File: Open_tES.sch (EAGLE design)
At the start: 60 parts, among them IC2 MAX232ECWES, IC4 LP2950CZ-5.0, IC5 OPA277U, IC6 LF444CM, IC7 PIC16F1937P, J1 RJ11-2X, U1 MIC2288YD5-TR, U2 74LVC1G10W6-7, X1 22-23-2041, X2 057-016-1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

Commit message: Removing input capacitor for LPO: C1_MIC already present.
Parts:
- removed C_LPO1: 1µF, rcl:C-EUC0805
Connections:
- net +9V: no longer C_LPO1.1
- net GND: no longer C_LPO1.2
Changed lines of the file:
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@@
 </part>
 <part name="SUPPLY8" library="supply2" deviceset="+9V" device="" value="+9V"/>
-<part name="C_LPO1" library="rcl" deviceset="C-EU" device="C0805" value="1µF">
-<attribute name="OC_FARNELL" value="2496946"/>
-</part>
 <part name="C_LPO2" library="rcl" deviceset="C-EU" device="C0805" value="1µF">
 <attribute name="OC_FARNELL" value="2496946"/>
@@
 <instance part="J1" gate="G$1" x="289.56" y="137.16"/>
 <instance part="SUPPLY8" gate="G$1" x="25.4" y="236.22"/>
-<instance part="C_LPO1" gate="G$1" x="101.6" y="236.22" rot="MR0">
-<attribute name="OC_FARNELL" x="101.6" y="236.22" size="1.778" layer="96" rot="MR0" display="off"/>
-</instance>
 <instance part="C_LPO2" gate="G$1" x="127" y="223.52" rot="MR0">
 <attribute name="OC_FARNELL" x="127" y="223.52" size="1.778" layer="96" rot="MR0" display="off"/>
@@
 <segment>
 <wire x1="111.76" y1="233.68" x2="111.76" y2="215.9" width="0.1524" layer="91"/>
-<wire x1="111.76" y1="215.9" x2="101.6" y2="215.9" width="0.1524" layer="91"/>
-<wire x1="101.6" y1="215.9" x2="101.6" y2="231.14" width="0.1524" layer="91"/>
 <wire x1="127" y1="218.44" x2="127" y2="215.9" width="0.1524" layer="91"/>
 <wire x1="127" y1="215.9" x2="111.76" y2="215.9" width="0.1524" layer="91"/>
@@
 <pinref part="GND19" gate="1" pin="GND"/>
 <pinref part="IC4" gate="G$1" pin="GND"/>
-<pinref part="C_LPO1" gate="G$1" pin="2"/>
 <pinref part="C_LPO2" gate="G$1" pin="2"/>
 </segment>
@@
 <pinref part="IC4" gate="G$1" pin="IN"/>
 <wire x1="96.52" y1="243.84" x2="96.52" y2="241.3" width="0.1524" layer="91"/>
-<wire x1="96.52" y1="241.3" x2="101.6" y2="241.3" width="0.1524" layer="91"/>
+<wire x1="96.52" y1="241.3" x2="104.14" y2="241.3" width="0.1524" layer="91"/>
 <pinref part="SUPPLY5" gate="G$1" pin="+9V"/>
-<pinref part="C_LPO1" gate="G$1" pin="1"/>
-<wire x1="101.6" y1="241.3" x2="104.14" y2="241.3" width="0.1524" layer="91"/>
-<wire x1="101.6" y1="241.3" x2="101.6" y2="238.76" width="0.1524" layer="91"/>
-</segment>
-<segment>
+</segment>
+<segment>

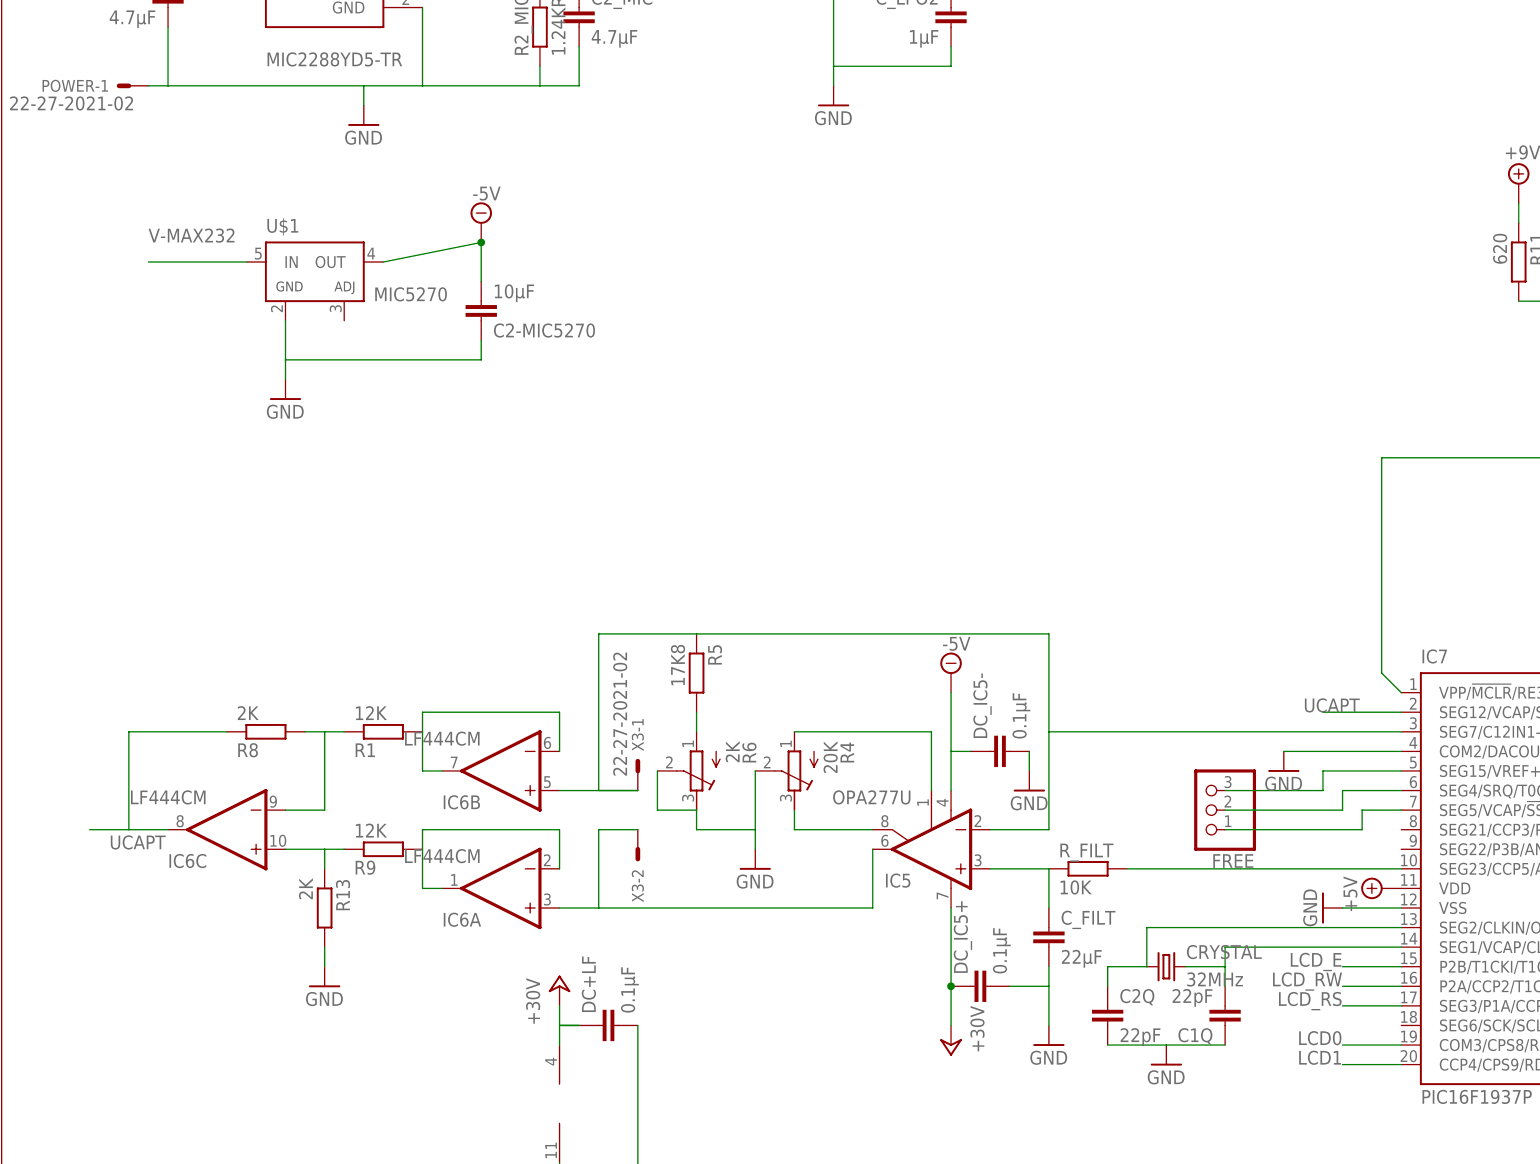
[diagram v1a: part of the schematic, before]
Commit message: Adding of state of charge module connecting to AN4: firmware updating is necessary. End of routing
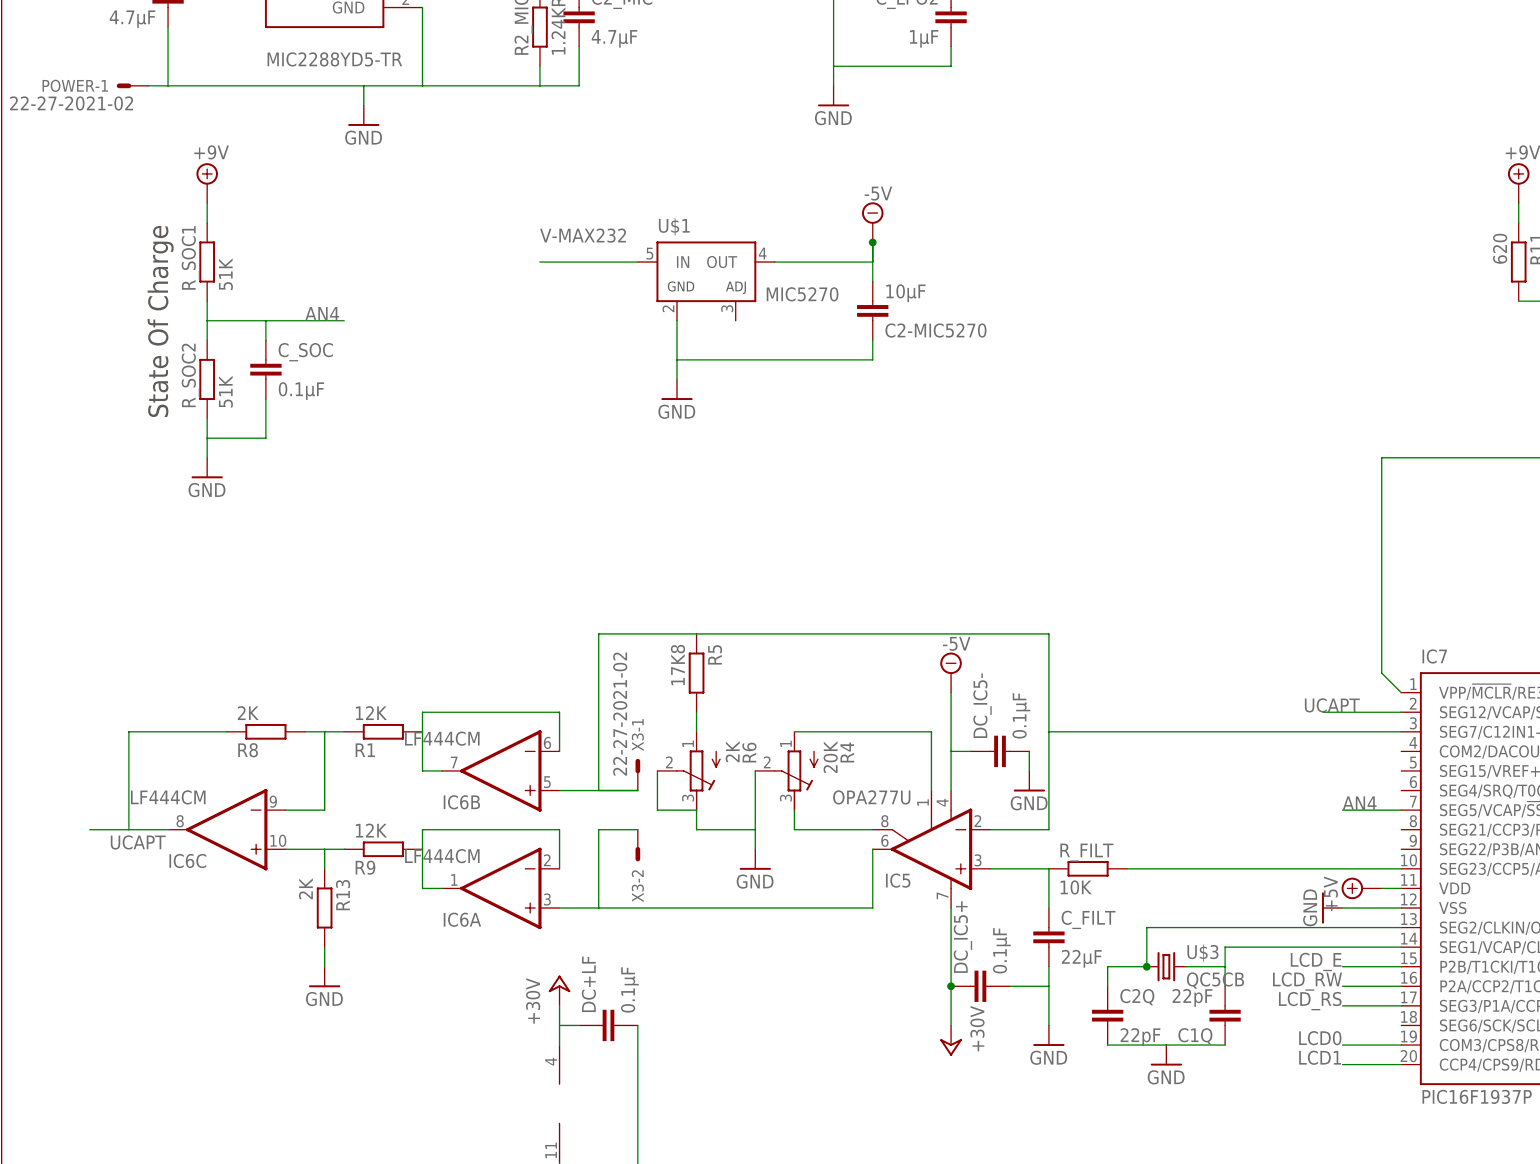
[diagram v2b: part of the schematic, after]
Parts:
- removed CRYSTAL: 32MHz, crystal:CRYSTALHC49U-V
- removed FREE: (no value), pinhead:PINHD-1X3
- added C_SOC: 0.1µF, rcl:C-EUC0805
- added R_SOC1, R_SOC2: 51K, rcl:R-EU_R0805
- added U$3: QC5CB, Open_tES:QC5CB
- C_FILT: device rcl:C-EUC1206 -> rcl:C-EUC0805
- R_LPO2: OC_FARNELL 2057662 -> 2057662
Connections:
- net +24V renamed +30V
- removed net N$24: FREE.1, IC7.SEG5/VCAP/!SS!/SRNQ/CPS7/C2OUT/AN4/RA5
- removed net N$26: FREE.2, IC7.SEG4/SRQ/T0CKI/CPS6/C1OUT/RA4
- removed net N$34: FREE.3, IC7.SEG15/VREF+/C1IN+/AN3/RA3
- new net AN4: C_SOC.1, IC7.SEG5/VCAP/!SS!/SRNQ/CPS7/C2OUT/AN4/RA5, R_SOC1.1, R_SOC2.2
- net +9V: now also R_SOC1.2
- net GND: now also C_SOC.2, R_SOC2.1; no longer IC7.COM2/DACOUT/VREF-/C2IN+/AN2/RA2
- net N$20: now also U$3.1; no longer CRYSTAL.1
- net N$6: now also U$3.2; no longer CRYSTAL.2
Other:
- note added: "State Of Charge"
- moved on the sheet: C2-MIC5270, U$1

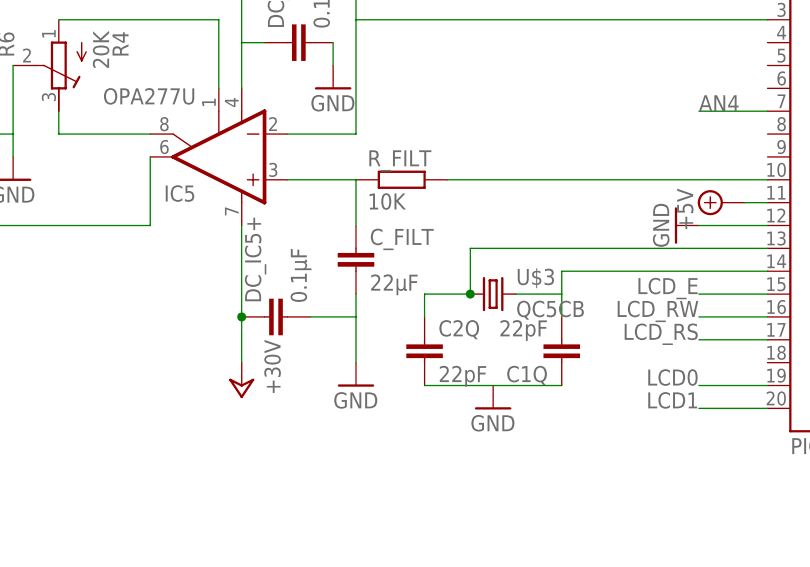
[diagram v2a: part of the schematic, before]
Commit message: Changing of C_FILT value 22->10uc to simplify the circuit. The same capacitor is already used on the board : C2-MIC5270
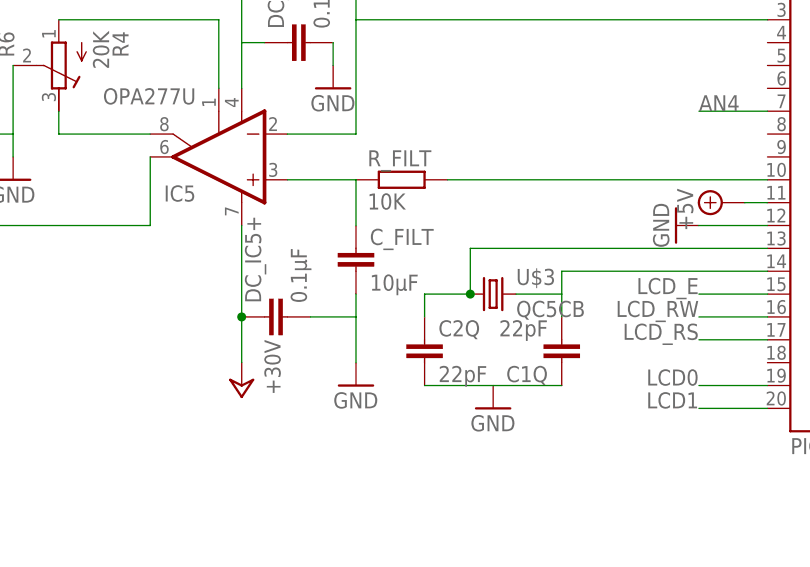
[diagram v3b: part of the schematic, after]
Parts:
- C1Q, C2Q: OC_FARNELL 1856180RL -> 1856180
- C1_PUSH, C2_PUSH, C3_PUSH: OC_FARNELL 1414662RL -> 1414662
- C2_MIC: OC_FARNELL 2458302 -> 2426962
- C_FILT: value 22µF -> 10µF; OC_FARNELL 499365 -> 2346934
- POWER: FARNELL 143126+1654528+1462641 -> (none)
- R1_MIC: OC_FARNELL 2303698 -> 1167459
- R5: OC_FARNELL 1811059 -> 1575931
- R_FILT: OC_FARNELL 2129113 -> 9332383
- X2: OC_FARNELL 8395934 -> 1554029
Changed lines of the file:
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@@
 </part>
 <part name="C2Q" library="rcl" deviceset="C-EU" device="C0805" value="22pF">
-<attribute name="OC_FARNELL" value="1856180RL"/>
+<attribute name="OC_FARNELL" value="1856180"/>
 </part>
 <part name="GND1" library="supply1" deviceset="GND" device=""/>
@@
 </part>
 <part name="R5" library="rcl" deviceset="R-EU_" device="M0805" value="17K8">
-<attribute name="OC_FARNELL" value="1811059"/>
+<attribute name="OC_FARNELL" value="1575931"/>
 </part>
 <part name="GND9" library="supply1" deviceset="GND" device=""/>
@@
 </part>
 <part name="X2" library="con-panduit" deviceset="057-016-" device="1">
-<attribute name="OC_FARNELL" value="8395934"/>
+<attribute name="OC_FARNELL" value="1554029"/>
 </part>
 <part name="GND12" library="supply1" deviceset="GND" device=""/>
@@
 </part>
 <part name="C1Q" library="rcl" deviceset="C-EU" device="C0805" value="22pF">
-<attribute name="OC_FARNELL" value="1856180RL"/>
+<attribute name="OC_FARNELL" value="1856180"/>
 </part>
 <part name="POWER" library="con-molex" deviceset="22-?-02" device="27-2021">
-<attribute name="FARNELL" value="143126+1654528+1462641"/>
 <attribute name="OC_FARNELL" value="143126+1654528+1462641"/>
 </part>
@@
 </part>
 <part name="C2_MIC" library="rcl" deviceset="C-EU" device="C0805" value="4.7µF">
-<attribute name="OC_FARNELL" value="2458302"/>
+<attribute name="OC_FARNELL" value="2426962"/>
 </part>
 <part name="SUPPLY3" library="supply2" deviceset="-5V" device="" value="-5V"/>
@@
 </part>
 <part name="C3_PUSH" library="rcl" deviceset="C-EU" device="C0805" value="0.01µF">
-<attribute name="OC_FARNELL" value="1414662RL"/>
+<attribute name="OC_FARNELL" value="1414662"/>
 </part>
 <part name="GND6" library="supply1" deviceset="GND" device=""/>
 <part name="C2_PUSH" library="rcl" deviceset="C-EU" device="C0805" value="0.01µF">
-<attribute name="OC_FARNELL" value="1414662RL"/>
+<attribute name="OC_FARNELL" value="1414662"/>
 </part>
 <part name="C1_PUSH" library="rcl" deviceset="C-EU" device="C0805" value="0.01µF">
-<attribute name="OC_FARNELL" value="1414662RL"/>
+<attribute name="OC_FARNELL" value="1414662"/>
 </part>
 <part name="GND16" library="supply1" deviceset="GND" device=""/>
 <part name="GND17" library="supply1" deviceset="GND" device=""/>
-<part name="C_FILT" library="rcl" deviceset="C-EU" device="C0805" value="22µF">
-<attribute name="OC_FARNELL" value="499365"/>
+<part name="C_FILT" library="rcl" deviceset="C-EU" device="C0805" value="10µF">
+<attribute name="OC_FARNELL" value="2346934"/>
 </part>
 <part name="R_FILT" library="rcl" deviceset="R-EU_" device="R0805" value="10K">
-<attribute name="OC_FARNELL" value="2129113"/>
+<attribute name="OC_FARNELL" value="9332383"/>
 </part>
 <part name="SUPPLY15" library="supply2" deviceset="+5V/1" device="" value="+5V"/>
@@
 </part>
 <part name="R1_MIC" library="rcl" deviceset="R-EU_" device="R0805" value="28.7KR">
-<attribute name="OC_FARNELL" value="2303698"/>
+<attribute name="OC_FARNELL" value="1167459"/>
 </part>
 <part name="R2_MIC" library="rcl" deviceset="R-EU_" device="R0805" value="1.24KR">
@@
 <attribute name="OC_FARNELL" x="162.56" y="91.44" size="1.778" layer="96" rot="R180" display="off"/>
 </instance>
-<instance part="POWER" gate="-1" x="20.32" y="213.36" rot="R180">
-<attribute name="FARNELL" x="20.32" y="213.36" size="1.778" layer="96" rot="R180" display="off"/>
-</instance>
+<instance part="POWER" gate="-1" x="20.32" y="213.36" rot="R180"/>
 <instance part="POWER" gate="-2" x="20.32" y="233.68" rot="R180"/>
 <instance part="SUPPLY5" gate="G$1" x="96.52" y="246.38"/>

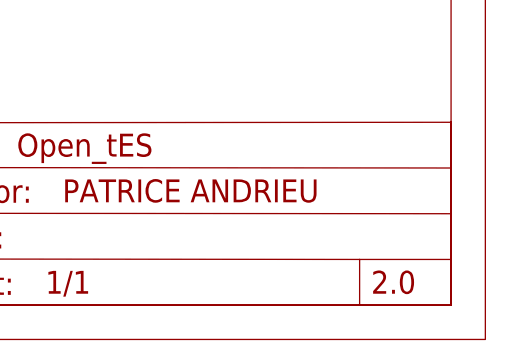
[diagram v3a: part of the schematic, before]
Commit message: replace package of R1 R8 R9 R13 MELF->0805 to reduce the cost. Update version 2.0->2.1 in files
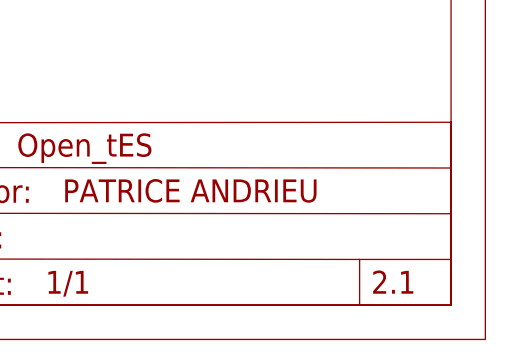
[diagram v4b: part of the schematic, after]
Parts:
- DC+LF: OC_FARNELL 1414664 -> 1653290
- R1: device rcl:R-EU_M1406 -> rcl:R-EU_R0805; OC_FARNELL 3086203 -> 1653290
- R13, R8: device rcl:R-EU_M1406 -> rcl:R-EU_R0805; OC_FARNELL 3086010 -> 1653296
- R9: device rcl:R-EU_M1406 -> rcl:R-EU_R0805
- U$4: VERSION 2.0 -> 2.1
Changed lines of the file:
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@@
 </part>
 <part name="GND29" library="supply1" deviceset="GND" device=""/>
-<part name="R1" library="rcl" deviceset="R-EU_" device="M1406" value="12K">
+<part name="R1" library="rcl" deviceset="R-EU_" device="R0805" value="12K">
+<attribute name="OC_FARNELL" value="1653290"/>
+</part>
+<part name="R9" library="rcl" deviceset="R-EU_" device="R0805" value="12K">
 <attribute name="OC_FARNELL" value="3086203"/>
 </part>
-<part name="R9" library="rcl" deviceset="R-EU_" device="M1406" value="12K">
-<attribute name="OC_FARNELL" value="3086203"/>
+<part name="R13" library="rcl" deviceset="R-EU_" device="R0805" value="2K">
+<attribute name="OC_FARNELL" value="1653296"/>
 </part>
-<part name="R13" library="rcl" deviceset="R-EU_" device="M1406" value="2K">
-<attribute name="OC_FARNELL" value="3086010"/>
-</part>
-<part name="R8" library="rcl" deviceset="R-EU_" device="M1406" value="2K">
-<attribute name="OC_FARNELL" value="3086010"/>
+<part name="R8" library="rcl" deviceset="R-EU_" device="R0805" value="2K">
+<attribute name="OC_FARNELL" value="1653296"/>
 </part>
 <part name="C1Q" library="rcl" deviceset="C-EU" device="C0805" value="22pF">
@@
 <part name="GND20" library="supply1" deviceset="GND" device=""/>
 <part name="DC+LF" library="rcl" deviceset="C-EU" device="C0805" value="0.1µF">
-<attribute name="OC_FARNELL" value="1414664"/>
+<attribute name="OC_FARNELL" value="1653290"/>
 </part>
 <part name="DC-LF" library="rcl" deviceset="C-EU" device="C0805" value="0.1µF">
@@
 <part name="GND7" library="supply1" deviceset="GND" device=""/>
 <part name="U$4" library="Open_tES" deviceset="FRAME" device="">
-<attribute name="VERSION" value="2.0"/>
+<attribute name="VERSION" value="2.1"/>
 </part>
 <part name="U1" library="Open_tES" deviceset="MIC2288YD5-TR" device="">

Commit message: Fixing of several mistakes concerning component references. Changing of package for the trimmers R4 R6.
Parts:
- POWER, X3: OC_FARNELL 143126+1654528+1462641 -> 9731148+1654528+1462641
- R4, R6: device rcl:R-TRIMM3224X -> rcl:R-TRIMM3214W
- R9: OC_FARNELL 3086203 -> 1653290
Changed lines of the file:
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@@
 <part name="SUPPLY1" library="supply2" deviceset="+5V/1" device="" value="+5V"/>
 <part name="X3" library="con-molex" deviceset="22-?-02" device="27-2021">
-<attribute name="OC_FARNELL" value="143126+1654528+1462641"/>
+<attribute name="OC_FARNELL" value="9731148+1654528+1462641"/>
 </part>
 <part name="X2" library="con-panduit" deviceset="057-016-" device="1">
@@
 </part>
 <part name="R9" library="rcl" deviceset="R-EU_" device="R0805" value="12K">
-<attribute name="OC_FARNELL" value="3086203"/>
+<attribute name="OC_FARNELL" value="1653290"/>
 </part>
 <part name="R13" library="rcl" deviceset="R-EU_" device="R0805" value="2K">
@@
 </part>
 <part name="POWER" library="con-molex" deviceset="22-?-02" device="27-2021">
-<attribute name="OC_FARNELL" value="143126+1654528+1462641"/>
+<attribute name="OC_FARNELL" value="9731148+1654528+1462641"/>
 </part>
 <part name="SUPPLY5" library="supply2" deviceset="+9V" device="" value="+9V"/>
@@
 <attribute name="OC_FARNELL" value="1502726"/>
 </part>
-<part name="R6" library="rcl" deviceset="R-TRIMM" device="3224X" value="2K">
+<part name="R6" library="rcl" deviceset="R-TRIMM" device="3214W" value="2K">
 <attribute name="OC_FARNELL" value="988250"/>
 </part>
@@
 </part>
 <part name="GND11" library="supply1" deviceset="GND" device=""/>
-<part name="R4" library="rcl" deviceset="R-TRIMM" device="3224X" value="20K">
+<part name="R4" library="rcl" deviceset="R-TRIMM" device="3214W" value="20K">
 <attribute name="OC_FARNELL" value="988285"/>
 </part>
